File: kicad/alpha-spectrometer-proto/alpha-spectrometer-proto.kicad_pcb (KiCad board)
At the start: 2 copper layers, 54.6 x 21.5 mm, 78 parts, among them J1 USB_B_Micro, J13 Anode, J14 Catode, J19 Conn, J2 Conn_01x01_Female, J20 Conn_01x01_Female, J21 Conn_01x01_Female, J22 Conn_01x01_Female, J3 Conn_01x01_Female, J4 BAT+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

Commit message: удалено:       kicad/alpha-spectrometer-proto/alpha-spectrometer-proto-backups/alpha-spectrometer-proto-2024-11-04_113452.zip 	изменено:      kicad/alpha-spectrometer-proto/alpha-spectrometer-proto.kicad_pcb 	изменено:      kicad/alpha-spectrometer-proto/alpha-spectrometer-proto.kicad_prl 	изменено:      kicad/alpha-spectrometer-proto/alpha-spectrometer-proto.kicad_sch
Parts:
- L1: footprint Inductor_SMD:L_1206_3216Metric -> Inductor_SMD:L_1206_3216Metric_Pad1.42x1.75mm_HandSolder
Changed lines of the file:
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@@
     )
   )
-  (footprint "Inductor_SMD:L_1206_3216Metric" (layer "B.Cu")
+  (footprint "Inductor_SMD:L_1206_3216Metric_Pad1.42x1.75mm_HandSolder" (layer "B.Cu")
     (at 92.92 46.35 180)
-    (descr "Inductor SMD 1206 (3216 Metric), square (rectangular) end terminal, IPC_7351 nominal, (Body size source: IPC-SM-782 page 80, https://www.pcb-3d.com/wordpress/wp-content/uploads/ipc-sm-782a_amendment_1_and_2.pdf), generated with kicad-footprint-generator")
-    (tags "inductor")
+    (descr "Inductor SMD 1206 (3216 Metric), square (rectangular) end terminal, IPC_7351 nominal with elongated pad for handsoldering. (Body size source: http://www.tortai-tech.com/upload/download/2011102023233369053.pdf), generated with kicad-footprint-generator")
+    (tags "inductor handsolder")
     (property "Sheetfile" "alpha-spectrometer-proto.kicad_sch")
     (property "Sheetname" "")
     (attr smd)
-    (fp_text reference "L1" (at 0 1.9) (layer "B.SilkS")
+    (fp_text reference "L1" (at 0 1.82) (layer "B.SilkS")
       (effects (font (size 1 1) (thickness 0.15)) (justify mirror))
     )
-    (fp_text value "22uH" (at 0 -1.9) (layer "B.Fab")
+    (fp_text value "22uH" (at 0 -1.82) (layer "B.Fab")
       (effects (font (size 1 1) (thickness 0.15)) (justify mirror))
     )
@@
       (effects (font (size 0.8 0.8) (thickness 0.12)) (justify mirror))
     )
-    (fp_line (start -0.835242 0.91) (end 0.835242 0.91) (layer "B.SilkS") (width 0.12))
-    (fp_line (start -0.835242 -0.91) (end 0.835242 -0.91) (layer "B.SilkS") (width 0.12))
-    (fp_line (start -2.35 -1.2) (end -2.35 1.2) (layer "B.CrtYd") (width 0.05))
-    (fp_line (start 2.35 1.2) (end 2.35 -1.2) (layer "B.CrtYd") (width 0.05))
-    (fp_line (start -2.35 1.2) (end 2.35 1.2) (layer "B.CrtYd") (width 0.05))
-    (fp_line (start 2.35 -1.2) (end -2.35 -1.2) (layer "B.CrtYd") (width 0.05))
+    (fp_line (start -0.602064 -0.91) (end 0.602064 -0.91) (layer "B.SilkS") (width 0.12))
+    (fp_line (start -0.602064 0.91) (end 0.602064 0.91) (layer "B.SilkS") (width 0.12))
+    (fp_line (start 2.45 1.12) (end 2.45 -1.12) (layer "B.CrtYd") (width 0.05))
+    (fp_line (start -2.45 1.12) (end 2.45 1.12) (layer "B.CrtYd") (width 0.05))
+    (fp_line (start 2.45 -1.12) (end -2.45 -1.12) (layer "B.CrtYd") (width 0.05))
+    (fp_line (start -2.45 -1.12) (end -2.45 1.12) (layer "B.CrtYd") (width 0.05))
+    (fp_line (start -1.6 -0.8) (end -1.6 0.8) (layer "B.Fab") (width 0.1))
+    (fp_line (start 1.6 0.8) (end 1.6 -0.8) (layer "B.Fab") (width 0.1))
+    (fp_line (start -1.6 0.8) (end 1.6 0.8) (layer "B.Fab") (width 0.1))
     (fp_line (start 1.6 -0.8) (end -1.6 -0.8) (layer "B.Fab") (width 0.1))
-    (fp_line (start 1.6 0.8) (end 1.6 -0.8) (layer "B.Fab") (width 0.1))
-    (fp_line (start -1.6 -0.8) (end -1.6 0.8) (layer "B.Fab") (width 0.1))
-    (fp_line (start -1.6 0.8) (end 1.6 0.8) (layer "B.Fab") (width 0.1))
-    (pad "1" smd roundrect (at -1.575 0 180) (size 1.05 1.9) (layers "B.Cu" "B.Paste" "B.Mask") (roundrect_rratio 0.238095)
+    (pad "1" smd roundrect (at -1.4875 0 180) (size 1.425 1.75) (layers "B.Cu" "B.Paste" "B.Mask") (roundrect_rratio 0.175439)
       (net 12 "BAT+") (pinfunction "1") (pintype "passive"))
-    (pad "2" smd roundrect (at 1.575 0 180) (size 1.05 1.9) (layers "B.Cu" "B.Paste" "B.Mask") (roundrect_rratio 0.238095)
+    (pad "2" smd roundrect (at 1.4875 0 180) (size 1.425 1.75) (layers "B.Cu" "B.Paste" "B.Mask") (roundrect_rratio 0.175439)
       (net 15 "Net-(D1-Pad2)") (pinfunction "2") (pintype "passive"))
     (model "${KICAD6_3DMODEL_DIR}/Inductor_SMD.3dshapes/L_1206_3216Metric.wrl"

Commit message: удалено:       Documents/mr107+-1.png 	удалено:       Documents/mr107+-10.png 	удалено:       Documents/mr107+-11.png 	удалено:       Documents/mr107+-12.png 	удалено:       Documents/mr107+-13.png 	удалено:       Documents/mr107+-14.png 	удалено:       Documents/mr107+-2.png 	удалено:       Documents/mr107+-3.png 	удалено:       Documents/mr107+-4.png 	удалено:       Documents/mr107+-5.png 	удалено:       Documents/mr107+-6.png 	удалено:       Documents/mr107+-7.png 	удалено:       Documents/mr107+-8.png 	удалено:       Documents/mr107+-9.png 	изменено:      GNUPlot/mainChart-1.gp 	изменено:      GNUPlot/mainChart-1.gp~ 	изменено:      STM32CubeIDE/TestController/.settings/language.settings.xml 	изменено:      STM32CubeIDE/TestController/Core/Src/main.c 	изменено:      STM32CubeIDE/TestController/Debug/Core/Src/main.o 	изменено:      STM32CubeIDE/TestController/Debug/TestController.elf 	изменено:      STM32CubeIDE/TestController/Debug/TestController.list 	изменено:      STM32CubeIDE/TestController/TestController.ioc 	удалено:       kicad/alpha-spectrometer-proto/alpha-spectrometer-proto-backups/alpha-spectrometer-proto-2024-10-29_185625.zip 	удалено:       kicad/alpha-spectrometer-proto/alpha-spectrometer-proto-backups/alpha-spectrometer-proto-2024-10-29_190534.zip 	удалено:       kicad/alpha-spectrometer-proto/alpha-spectrometer-proto-backups/alpha-spectrometer-proto-2024-10-30_170209.zip 	удалено:       kicad/alpha-spectrometer-proto/alpha-spectrometer-proto-backups/alpha-spectrometer-proto-2024-10-30_171711.zip 	удалено:       kicad/alpha-spectrometer-proto/alpha-spectrometer-proto-backups/alpha-spectrometer-proto-2024-10-30_184706.zip 	удалено:       kicad/alpha-spectrometer-proto/alpha-spectrometer-proto-backups/alpha-spectrometer-proto-2024-10-30_185305.zip 	удалено:       kicad/alpha-spectrometer-proto/alpha-spectrometer-proto-backups/alpha-spectrometer-proto-2024-10-30_190038.zip 	удалено:       kicad/alpha-spectrometer-proto/alpha-spectrometer-proto-backup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
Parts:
- removed C14: 10, Capacitor_SMD:C_0603_1608Metric
- removed C15: 100n, Capacitor_SMD:C_0603_1608Metric
- removed C17: 10u, Capacitor_SMD:C_0603_1608Metric
- removed D3: AD5245, Package_TO_SOT_SMD:SOT-23-8_Handsoldering
- added R15: 10, Resistor_SMD:R_0603_1608Metric, F.Cu at (77.2, 55.5)
- added U4: AD8605, Package_TO_SOT_SMD:TSOT-23-5, F.Cu at (77.8, 44.0)
- C22: moved to F.Cu
- C3: value 1n -> 100p
- C4: value 10n -> 100n
- C5: value 10 -> 4.7
- C6: value 100n -> 10u; moved to F.Cu
- R1: value 10k -> 100k; moved to F.Cu
- R18: value 100k -> 51k; moved to F.Cu
- R2: value 10k -> 20k
- R5: value 10k -> 1k
- R6: value 5.1M -> 2M
- moved C6 14.8 mm to (78.0, 41.8)
- moved R12 5.06 mm to (82.4, 41.6)
- moved C22 4.01 mm to (80.2, 40.6), turned to -90 degrees
- moved R5 2.90 mm to (70.2, 46.0)
- moved R1 1.23 mm to (63.5, 49.6), turned to 0 degrees
- moved R18 0.96 mm to (77.5, 46.4)
- moved C2 0.90 mm to (63.5, 47.6), turned to 180 degrees
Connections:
- C6 pad 1: Net-(C5-Pad2) -> GND
- C6 pad 2: Net-(C6-Pad2) -> +3V3
- R18 pad 1: GND -> Net-(R18-Pad1)
- R18 pad 2: Net-(C15-Pad2) -> Net-(R18-Pad2)
- R5 pad 1: Net-(C14-Pad1) -> Net-(C5-Pad2)
- R5 pad 2: GND -> Net-(R5-Pad2)
- R6 pad 1: Net-(C14-Pad1) -> Net-(R5-Pad2)
- R6 pad 2: Analog -> Net-(R18-Pad2)
- U1 pad 1: Analog -> Net-(R18-Pad2)
- U1 pad 2: Net-(C14-Pad1) -> Net-(R5-Pad2)
- U1 pad 3: Net-(D3-Pad1) -> Net-(C4-Pad2)
- U5 pad 3: Net-(C15-Pad2) -> Net-(R18-Pad1)
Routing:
- net scl: track 43.8 -> 0.00 mm
- net sda: track 42.7 -> 0.00 mm
- net Analog: track 54.2 -> 33.4 mm, vias 5 -> 2
- net Net-(R15-Pad2): track 0.00 -> 13.6 mm
- net Net-(R18-Pad2): track 0.00 -> 12.3 mm, vias 0 -> 1
- net Net-(C5-Pad2): track 5.42 -> 13.0 mm
- net +5VA: track 31.1 -> 24.1 mm, vias 7 -> 6
- net Net-(C15-Pad2): track 6.88 -> 0.00 mm
- net GND: track 120.6 -> 114.4 mm, vias 32 -> 35
- net Net-(C6-Pad2): track 5.83 -> 0.00 mm, vias 1 -> 0
- net Net-(C14-Pad1): track 4.99 -> 0.00 mm
- net Net-(C4-Pad2): track 4.43 -> 9.03 mm, vias 0 -> 2
- net Net-(D5-Pad14): track 49.2 -> 44.7 mm
- net Net-(R5-Pad2): track 0.00 -> 3.83 mm
- net +3V3: track 63.2 -> 66.4 mm
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
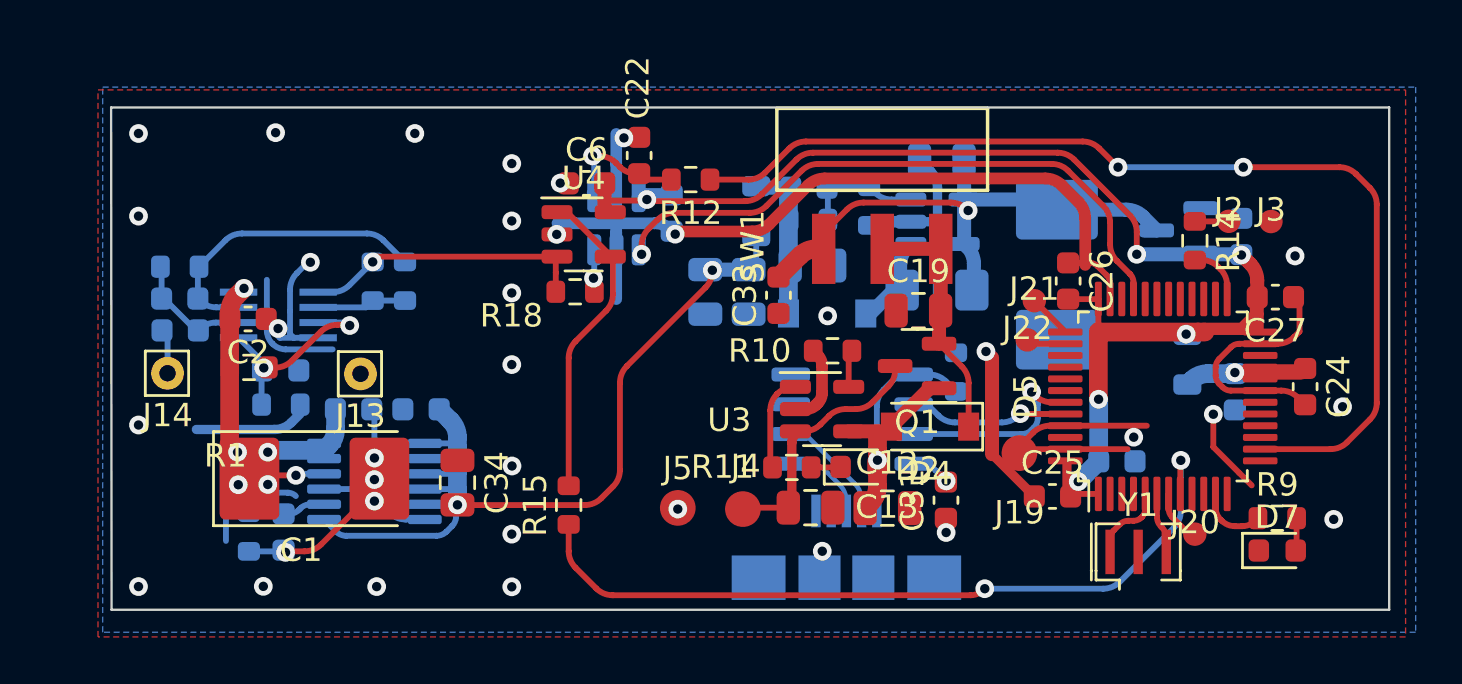
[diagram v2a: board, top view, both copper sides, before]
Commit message: изменено:      STM32CubeIDE/TestController/.mxproject 	изменено:      STM32CubeIDE/TestController/.settings/language.settings.xml 	изменено:      STM32CubeIDE/TestController/Core/Inc/main.h 	изменено:      STM32CubeIDE/TestController/Core/Src/main.c 	изменено:      STM32CubeIDE/TestController/Core/Src/stm32g4xx_hal_msp.c 	изменено:      STM32CubeIDE/TestController/TestController.ioc 	удалено:       kicad/alpha-spectrometer-proto/alpha-spectrometer-proto-backups/alpha-spectrometer-proto-2024-10-31_190535.zip 	удалено:       kicad/alpha-spectrometer-proto/alpha-spectrometer-proto-backups/alpha-spectrometer-proto-2024-11-02_112209.zip 	удалено:       kicad/alpha-spectrometer-proto/alpha-spectrometer-proto-backups/alpha-spectrometer-proto-2024-11-03_173252.zip 	удалено:       kicad/alpha-spectrometer-proto/alpha-spectrometer-proto-backups/alpha-spectrometer-proto-2024-11-03_174252.zip 	удалено:       kicad/alpha-spectrometer-proto/alpha-spectrometer-proto-backups/alpha-spectrometer-proto-2024-11-03_175253.zip 	удалено:       kicad/alpha-spectrometer-proto/alpha-spectrometer-proto-backups/alpha-spectrometer-proto-2024-11-03_175855.zip 	удалено:       kicad/alpha-spectrometer-proto/alpha-spectrometer-proto-backups/alpha-spectrometer-proto-2024-11-03_201807.zip 	удалено:       kicad/alpha-spectrometer-proto/alpha-spectrometer-proto-backups/alpha-spectrometer-proto-2024-11-04_114242.zip 	удалено:       kicad/alpha-spectrometer-proto/alpha-spectrometer-proto-backups/alpha-spectrometer-proto-2024-11-04_115247.zip 	удалено:       kicad/alpha-spectrometer-proto/alpha-spectrometer-proto-backups/alpha-spectrometer-proto-2024-11-04_122306.zip 	изменено:      kicad/alpha-spectrometer-proto/alpha-spectrometer-proto.kicad_pcb 	изменено:      kicad/alpha-spectrometer-proto/alpha-spectrometer-proto.kicad_prl 	изменено:      kicad/alpha-spectrometer-proto/alpha-spectrometer-proto.kicad_pro 	изменено:      kicad/alpha-spectrometer-proto/alpha-spectrometer-proto.kicad_sch
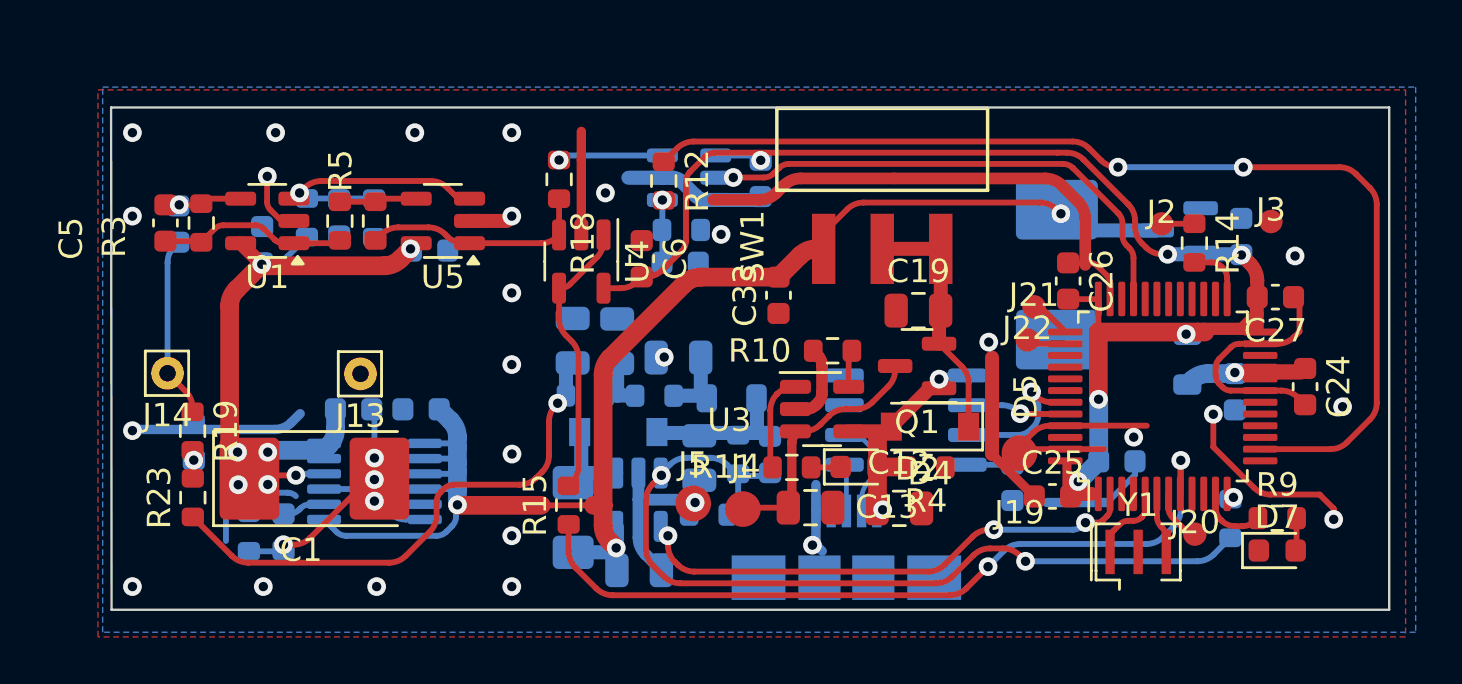
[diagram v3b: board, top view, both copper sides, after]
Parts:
- removed C10, C11, C34, C9: 10u, Capacitor_SMD:C_0805_2012Metric
- removed C8: 220p, Capacitor_SMD:C_0603_1608Metric
- removed D1: MBR0540, Diode_SMD:D_SOD-123
- removed L1: 22uH, Inductor_SMD:L_1206_3216Metric_Pad1.42x1.75mm_HandSolder
- removed L2: 47uH, Inductor_SMD:L_0805_2012Metric
- removed R8: 13.3k, Resistor_SMD:R_0603_1608Metric
- removed U2: LM2733XMF, Package_TO_SOT_SMD:SOT-23-5
- added C14: 10u, Capacitor_SMD:C_0805_2012Metric, B.Cu at (80.2, 58.3)
- added C15: 220p, Capacitor_SMD:C_0603_1608Metric, B.Cu at (85.8, 53.4)
- added C17: 10u, Capacitor_SMD:C_0805_2012Metric, B.Cu at (82.8, 53.5)
- added C29: 10u, Capacitor_SMD:C_0805_2012Metric, B.Cu at (81.9, 49.2)
- added C35: 10u, Capacitor_SMD:C_0805_2012Metric, B.Cu at (79.3, 48.5)
- added C36: 10u, Capacitor_SMD:C_0805_2012Metric, B.Cu at (77.4, 48.5)
- added C37: 10u, Capacitor_SMD:C_0603_1608Metric, B.Cu at (61.2, 52.8)
- added D3: MBR0540, Diode_SMD:D_SOD-123, B.Cu at (79.3, 52.4)
- added L4: 22uH, Inductor_SMD:L_1206_3216Metric_Pad1.42x1.75mm_HandSolder, B.Cu at (77.4, 56.1)
- added L5: 47uH, Inductor_SMD:L_0805_2012Metric, B.Cu at (84.2, 51.0)
- added R16: 117k, Resistor_SMD:R_0603_1608Metric, B.Cu at (84.4, 53.4)
- added R17: 5.1k, Resistor_SMD:R_0603_1608Metric, B.Cu at (83.2, 55.9)
- added R19: 10M, Resistor_SMD:R_0603_1608Metric, F.Cu at (61.1, 52.4)
- added R20: 50k, Resistor_SMD:R_0603_1608Metric, B.Cu at (105.5, 56.1)
- added R21: 20k, Resistor_SMD:R_0603_1608Metric, B.Cu at (80.8, 50.9)
- added R22: 20k, Resistor_SMD:R_0603_1608Metric, B.Cu at (77.9, 50.9)
- added R23: 1.5M, Resistor_SMD:R_0603_1608Metric, F.Cu at (61.1, 55.2)
- added U8: LM2733XMF, Package_TO_SOT_SMD:SOT-23-5, B.Cu at (80.2, 55.3)
- added U9: TLV3501AIDBV, Package_TO_SOT_SMD:SOT-23-6, B.Cu at (82.3, 41.5)
- C2, C22, C31: moved to B.Cu
- C5: value 4.7 -> 4.7p; moved to F.Cu
- C7: footprint Capacitor_SMD:C_0805_2012Metric -> Capacitor_SMD:C_0603_1608Metric
- R1: value 100k -> 10k; moved to B.Cu
- R2: value 20k -> 100k
- R3, R4, R5, R6: moved to F.Cu
- R7: value 117k -> 1k
- U1: value MAX4477 -> AD8061; footprint Package_SO:SSOP-8_2.95x2.8mm_P0.65mm -> Package_TO_SOT_SMD:TSOT-23-5; moved to F.Cu
- U4: value AD8605 -> AD8061
- U5: value LMV7239 -> AD8061; footprint Package_TO_SOT_SMD:SOT-23-5 -> Package_TO_SOT_SMD:TSOT-23-5; moved to F.Cu
- moved C7 22.2 mm to (71.2, 44.7), turned to 180 degrees
- moved R2 8.91 mm to (68.9, 43.3), turned to -90 degrees
- moved U5 7.41 mm to (71.8, 43.4), turned to 180 degrees
- moved C4 6.98 mm to (67.4, 43.3), turned to 90 degrees
- moved R1 6.85 mm to (66.0, 43.3), turned to 90 degrees
- moved R7 5.45 mm to (82.0, 43.8)
- moved C22 4.90 mm to (82.0, 45.2), turned to 180 degrees
- moved R18 4.85 mm to (76.8, 41.6), turned to -90 degrees
- moved C3 4.54 mm to (60.5, 43.5), turned to 90 degrees
- moved R4 4.27 mm to (92.5, 53.9), turned to 180 degrees
- moved C32 4.08 mm to (85.4, 41.6)
- moved U1 4.04 mm to (64.3, 43.4)
- moved C6 3.99 mm to (80.3, 45.0), turned to -90 degrees
- moved R5 3.79 mm to (67.4, 43.4), turned to 90 degrees
- moved C5 3.28 mm to (60.0, 43.5), turned to -90 degrees
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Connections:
- C1 pad 1: +5VA -> +3.3VA
- C16 pad 2: +12V -> BAT+
- C2 pad 2: +5VA -> +3.3VA
- C20 pad 2: +5VA -> +3.3VA
- C3 pad 2: Net-(C3-Pad2) -> Net-(U1--)
- C4 pad 2: Net-(C4-Pad2) -> offset
- C5 pad 1: Net-(C3-Pad2) -> Net-(U1--)
- C7 pad 2: BAT+ -> +3.3VA
- D5 pad 12: unconnected-(D5-Pad12) -> AdjHV
- D5 pad 2: unconnected-(D5-Pad2) -> HVEnable
- R1 pad 1: +5VA -> +3.3VA
- R1 pad 2: Net-(C4-Pad2) -> offset
- R18 pad 1: Net-(R18-Pad1) -> Net-(U9-+)
- R18 pad 2: Net-(R18-Pad2) -> Net-(U4-+)
- R2 pad 1: Net-(C4-Pad2) -> offset
- R3 pad 1: Net-(C3-Pad2) -> Net-(U1--)
- R5 pad 2: Net-(R5-Pad2) -> Net-(U5--)
- R6 pad 1: Net-(R5-Pad2) -> Net-(U5--)
- R6 pad 2: Net-(R18-Pad2) -> Net-(U4-+)
- R7 pad 1: Net-(C8-Pad2) -> Adj
- R7 pad 2: Net-(C8-Pad1) -> GND
- U1 pad 1: Net-(R18-Pad2) -> Net-(C5-Pad2)
- U1 pad 2: Net-(R5-Pad2) -> GND
- U1 pad 3: Net-(C4-Pad2) -> offset
- U1 pad 4: GND -> Net-(U1--)
- U1 pad 5: Net-(C4-Pad2) -> +3.3VA
- U4 pad 3: Net-(R18-Pad2) -> Net-(U4-+)
- U5 pad 1: Pulse -> Net-(U4-+)
- U5 pad 3: Net-(R18-Pad1) -> offset
- U5 pad 4: Adj -> Net-(U5--)
- U5 pad 5: +3V3 -> +3.3VA
- U7 pad 1: +12V -> BAT+
- U7 pad 10: +5VA -> +3.3VA
- U7 pad 11: +5VA -> +3.3VA
- U7 pad 12: +5VA -> +3.3VA
- U7 pad 2: +12V -> BAT+
- U7 pad 3: +12V -> BAT+
- U7 pad 4: +12V -> BAT+
- U7 pad 5: PowerGood -> unconnected-(U7-PG-Pad5)
- U7 pad 7: +12V -> BAT+
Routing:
- net +12V: track 38.3 -> 0.00 mm, vias 2 -> 0
- net BAT+: track 24.5 -> 62.4 mm, vias 1 -> 3
- net Net-(U8-FB): track 0.00 -> 37.1 mm, vias 0 -> 2
- net +3.3VA: track 0.00 -> 36.0 mm, vias 0 -> 7
- net +5VA: track 24.1 -> 0.00 mm, vias 6 -> 0
- net +30v: track 0.00 -> 23.2 mm, vias 0 -> 1
- net HVEnable: track 0.00 -> 21.6 mm, vias 0 -> 3
- net Net-(R18-Pad2): track 12.3 -> 0.00 mm, vias 1 -> 0
- net offset: track 0.00 -> 10.9 mm, vias 0 -> 1
- net Net-(U4-+): track 0.00 -> 9.85 mm
- net Net-(C4-Pad2): track 9.03 -> 0.00 mm, vias 2 -> 0
- net Net-(C8-Pad2): track 6.92 -> 0.00 mm
- net Net-(D3-K): track 0.00 -> 6.37 mm
- net VBUS: track 16.8 -> 10.6 mm, vias 1 -> 2
- net Net-(C3-Pad1): track 1.93 -> 7.78 mm
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- added copper zone on B.Cu, net +3.3VA
- removed copper zone on B.Cu, net +5VA
